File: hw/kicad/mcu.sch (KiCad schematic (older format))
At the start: 43 parts, among them P1 CONN_01X06, P2 CONN_01X03, P3 CONN_02X05, P4 CONN_01X05, SW1 PTS810, U1 STM32F446R(C-E)Tx, Y1 16 MHz

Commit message: work
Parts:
- added R43: 0R, Resistors_SMD:R_0402, symbol R
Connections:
- net +3V3: now also R43.1; no longer C9.1, U1.13 (VDDA/VREF+)
- net SWCLK: now reaches P4.2 (P2)
- net SWCLK: now also U1.49 (PA14/SYS_JTCK-SWCLK); no longer U1.46 (PA13/SYS_JTMS-SWDIO)
- net SWDIO: now reaches P4.4 (P4)
- net SWDIO: now also U1.46 (PA13/SYS_JTMS-SWDIO); no longer U1.49 (PA14/SYS_JTCK-SWCLK)
- net RST: now reaches C10.1, P4.5 (P5), U1.7 (NRST)
- new net I_SENS_V_REF: C9.1, R43.2, U1.13 (VDDA/VREF+)
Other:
- moved on the sheet: D5, D6, R12, R13, SW1
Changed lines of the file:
@@
 Text HLabel 3900 2800 0    60   Output ~ 0
 PWM_L_C
-Text HLabel 8750 4400 2    60   Output ~ 0
+Text HLabel 9300 4400 2    60   Output ~ 0
 I_SENS_V_REF
 Text HLabel 3900 4100 0    60   Input ~ 0
@@
 F 3 "" H 8550 4600 60  0000 C CNN
 	1    8550 4600
-	1    0    0    -1
-$EndComp
-$Comp
-L CONN_01X05 P4
-U 1 1 581756C8
-P 9750 1400
-F 0 "P4" H 9750 1700 50  0000 C CNN
-F 1 "CONN_01X05" V 9850 1400 50  0000 C CNN
-F 2 "Pin_Headers:Pin_Header_Straight_1x05" H 9750 1400 60  0001 C CNN
-F 3 "" H 9750 1400 60  0000 C CNN
-	1    9750 1400
-	1    0    0    -1
-$EndComp
-$Comp
-L +3.3V #PWR03
-U 1 1 58175A3D
-P 9450 950
-F 0 "#PWR03" H 9450 800 50  0001 C CNN
-F 1 "+3.3V" H 9450 1090 50  0000 C CNN
-F 2 "" H 9450 950 60  0000 C CNN
-F 3 "" H 9450 950 60  0000 C CNN
-	1    9450 950
 	1    0    0    -1
 $EndComp
@@
 	8350 4200 8200 4200
 Wire Wire Line
-	8350 3700 8350 4400
-Wire Wire Line
-	8200 3800 8350 3800
+	8200 3800 8550 3800
 Connection ~ 10000 5600
 Connection ~ 10000 6000
@@
 	8350 4900 8200 4900
 Wire Wire Line
-	8200 4400 8750 4400
-Connection ~ 8350 4200
-Wire Wire Line
-	8550 4400 8550 4450
-Connection ~ 8350 4400
+	8200 4400 9300 4400
+Wire Wire Line
+	8550 4350 8550 4450
 Connection ~ 8550 4400
 Wire Wire Line
-	8200 1300 9550 1300
-Wire Wire Line
-	9550 1200 9450 1200
-Wire Wire Line
-	9450 1200 9450 950
-Wire Wire Line
-	9550 1600 8900 1600
-Wire Wire Line
-	9450 1700 9450 1400
-Wire Wire Line
-	9450 1400 9550 1400
-Wire Wire Line
-	8900 1600 8900 1950
-Connection ~ 8900 1900
-Wire Wire Line
 	8900 2350 8900 2250
 Wire Wire Line
@@
 Wire Wire Line
 	8900 1900 8200 1900
-Wire Wire Line
-	8900 1500 9550 1500
-Wire Wire Line
-	8200 1400 8900 1400
-Wire Wire Line
-	8900 1400 8900 1500
 Wire Wire Line
 	8350 6100 8350 5950
@@
 	4700 1400 2950 1400
 Wire Wire Line
-	2950 1400 2950 2000
-Wire Wire Line
-	2950 2000 1800 2000
+	2950 2000 2950 1400
+Wire Wire Line
+	1800 2000 2950 2000
 Wire Wire Line
 	3050 2700 3050 1500
@@
 $EndComp
 $Comp
-L GND #PWR023
-U 1 1 58278102
-P 9450 1700
-F 0 "#PWR023" H 9450 1450 50  0001 C CNN
-F 1 "GND" H 9450 1550 50  0000 C CNN
-F 2 "" H 9450 1700 60  0000 C CNN
-F 3 "" H 9450 1700 60  0000 C CNN
-	1    9450 1700
-	1    0    0    -1
-$EndComp
-$Comp
 L R R1
 U 1 1 58291693
@@
 L LED D6
 U 1 1 58362F24
-P 10650 4850
-F 0 "D6" H 10650 4950 50  0000 C CNN
-F 1 "LED" H 10650 4750 50  0000 C CNN
-F 2 "LEDs:LED_0603" H 10650 4850 60  0001 C CNN
-F 3 "" H 10650 4850 60  0000 C CNN
-	1    10650 4850
+P 10550 3000
+F 0 "D6" H 10550 3100 50  0000 C CNN
+F 1 "LED" H 10550 2900 50  0000 C CNN
+F 2 "LEDs:LED_0603" H 10550 3000 60  0001 C CNN
+F 3 "" H 10550 3000 60  0000 C CNN
+	1    10550 3000
 	-1   0    0    1
 $EndComp
@@
 L LED D5
 U 1 1 583633B5
-P 10650 4550
-F 0 "D5" H 10650 4650 50  0000 C CNN
-F 1 "LED" H 10650 4450 50  0000 C CNN
-F 2 "LEDs:LED_0603" H 10650 4550 60  0001 C CNN
-F 3 "" H 10650 4550 60  0000 C CNN
-	1    10650 4550
+P 10550 2700
+F 0 "D5" H 10550 2800 50  0000 C CNN
+F 1 "LED" H 10550 2600 50  0000 C CNN
+F 2 "LEDs:LED_0603" H 10550 2700 60  0001 C CNN
+F 3 "" H 10550 2700 60  0000 C CNN
+	1    10550 2700
 	-1   0    0    1
 $EndComp
 Wire Wire Line
-	10850 4550 11000 4550
-Wire Wire Line
-	11000 4550 11000 4950
-Wire Wire Line
-	10850 4850 11000 4850
-Connection ~ 11000 4850
+	10750 2700 10900 2700
+Wire Wire Line
+	10900 2700 10900 3100
+Wire Wire Line
+	10750 3000 10900 3000
+Connection ~ 10900 3000
 $Comp
 L GND #PWR028
 U 1 1 58363604
-P 11000 4950
-F 0 "#PWR028" H 11000 4700 50  0001 C CNN
-F 1 "GND" H 11000 4800 50  0000 C CNN
-F 2 "" H 11000 4950 60  0000 C CNN
-F 3 "" H 11000 4950 60  0000 C CNN
-	1    11000 4950
+P 10900 3100
+F 0 "#PWR028" H 10900 2850 50  0001 C CNN
+F 1 "GND" H 10900 2950 50  0000 C CNN
+F 2 "" H 10900 3100 60  0000 C CNN
+F 3 "" H 10900 3100 60  0000 C CNN
+	1    10900 3100
 	1    0    0    -1
 $EndComp
@@
 L R R12
 U 1 1 58363C15
-P 10250 4550
-F 0 "R12" V 10330 4550 50  0000 C CNN
-F 1 "100R" V 10250 4550 50  0000 C CNN
-F 2 "Resistors_SMD:R_0402" V 10180 4550 30  0001 C CNN
-F 3 "" H 10250 4550 30  0000 C CNN
-	1    10250 4550
+P 10150 2700
+F 0 "R12" V 10230 2700 50  0000 C CNN
+F 1 "100R" V 10150 2700 50  0000 C CNN
+F 2 "Resistors_SMD:R_0402" V 10080 2700 30  0001 C CNN
+F 3 "" H 10150 2700 30  0000 C CNN
+	1    10150 2700
 	0    1    1    0
 $EndComp
@@
 L R R13
 U 1 1 58363D14
-P 10250 4850
-F 0 "R13" V 10330 4850 50  0000 C CNN
-F 1 "100R" V 10250 4850 50  0000 C CNN
-F 2 "Resistors_SMD:R_0402" V 10180 4850 30  0001 C CNN
-F 3 "" H 10250 4850 30  0000 C CNN
-	1    10250 4850
+P 10150 3000
+F 0 "R13" V 10230 3000 50  0000 C CNN
+F 1 "100R" V 10150 3000 50  0000 C CNN
+F 2 "Resistors_SMD:R_0402" V 10080 3000 30  0001 C CNN
+F 3 "" H 10150 3000 30  0000 C CNN
+	1    10150 3000
 	0    1    1    0
 $EndComp
 Wire Wire Line
-	10400 4850 10450 4850
-Wire Wire Line
-	10400 4550 10450 4550
-Text Label 9800 4550 0    60   ~ 0
+	10300 3000 10350 3000
+Wire Wire Line
+	10300 2700 10350 2700
+Text Label 9700 2700 0    60   ~ 0
 LED_R
 Wire Wire Line
-	9800 4550 10100 4550
-Wire Wire Line
-	10100 4850 9800 4850
-Text Label 9800 4850 0    60   ~ 0
+	9700 2700 10000 2700
+Wire Wire Line
+	10000 3000 9700 3000
+Text Label 9700 3000 0    60   ~ 0
 LED_G
 Wire Wire Line
@@
 L PTS810 SW1
 U 1 1 583BCE20
-P 10650 4100
-F 0 "SW1" H 10650 4200 40  0000 C CNN
-F 1 "PTS810" H 10650 4050 40  0000 C CNN
-F 2 "electromechanical:PTS810" H 10650 4100 60  0001 C CNN
-F 3 "" H 10650 4100 60  0000 C CNN
-	1    10650 4100
+P 10550 2250
+F 0 "SW1" H 10550 2350 40  0000 C CNN
+F 1 "PTS810" H 10550 2200 40  0000 C CNN
+F 2 "electromechanical:PTS810" H 10550 2250 60  0001 C CNN
+F 3 "" H 10550 2250 60  0000 C CNN
+	1    10550 2250
 	1    0    0    -1
 $EndComp
@@
 L GND #PWR034
 U 1 1 583BE21E
-P 11000 4200
-F 0 "#PWR034" H 11000 3950 50  0001 C CNN
-F 1 "GND" H 11000 4050 50  0000 C CNN
-F 2 "" H 11000 4200 60  0000 C CNN
-F 3 "" H 11000 4200 60  0000 C CNN
-	1    11000 4200
-	1    0    0    -1
-$EndComp
-Wire Wire Line
-	10750 4100 11000 4100
-Wire Wire Line
-	11000 4100 11000 4200
-Wire Wire Line
-	10550 4100 9800 4100
-Text Label 9800 4100 0    60   ~ 0
+P 10900 2350
+F 0 "#PWR034" H 10900 2100 50  0001 C CNN
+F 1 "GND" H 10900 2200 50  0000 C CNN
+F 2 "" H 10900 2350 60  0000 C CNN
+F 3 "" H 10900 2350 60  0000 C CNN
+	1    10900 2350
+	1    0    0    -1
+$EndComp
+Wire Wire Line
+	10650 2250 10900 2250
+Wire Wire Line
+	10900 2250 10900 2350
+Wire Wire Line
+	10450 2250 9700 2250
+Text Label 9700 2250 0    60   ~ 0
 BTN
+$Comp
+L GND #PWR?
+U 1 1 5842C05B
+P 10450 1400
+F 0 "#PWR?" H 10450 1150 50  0001 C CNN
+F 1 "GND" H 10450 1250 50  0000 C CNN
+F 2 "" H 10450 1400 60  0000 C CNN
+F 3 "" H 10450 1400 60  0000 C CNN
+	1    10450 1400
+	0    1    1    0
+$EndComp
+$Comp
+L +3.3V #PWR?
+U 1 1 5842C60A
+P 10400 1150
+F 0 "#PWR?" H 10400 1000 50  0001 C CNN
+F 1 "+3.3V" H 10400 1290 50  0000 C CNN
+F 2 "" H 10400 1150 60  0000 C CNN
+F 3 "" H 10400 1150 60  0000 C CNN
+	1    10400 1150
+	1    0    0    -1
+$EndComp
+Text Label 9950 1500 0    60   ~ 0
+SWDIO
+Text Label 9950 1300 0    60   ~ 0
+SWCLK
+Text Label 9950 1600 0    60   ~ 0
+RST
+Wire Wire Line
+	8900 1900 8900 1950
+Text Label 8800 1300 2    60   ~ 0
+SWDIO
+Text Label 8800 1400 2    60   ~ 0
+SWCLK
+Text Label 8800 1900 2    60   ~ 0
+RST
+Wire Wire Line
+	8200 1300 8800 1300
+Wire Wire Line
+	8200 1400 8800 1400
+$Comp
+L R R43
+U 1 1 58432E11
+P 8550 4200
+F 0 "R43" H 8700 4200 50  0000 C CNN
+F 1 "0R" V 8550 4200 50  0000 C CNN
+F 2 "Resistors_SMD:R_0402" V 8480 4200 30  0001 C CNN
+F 3 "" H 8550 4200 30  0000 C CNN
+	1    8550 4200
+	1    0    0    -1
+$EndComp
+Wire Wire Line
+	8350 3700 8350 4200
+Wire Wire Line
+	8550 3800 8550 4050
+Text Label 8650 4400 0    60   ~ 0
+I_SENS_V_REF
+$Comp
+L CONN_01X05 P4
+U 1 1 584386F1
+P 10650 1400
+F 0 "P4" H 10650 1700 50  0000 C CNN
+F 1 "CONN_01X05" V 10750 1400 50  0000 C CNN
+F 2 "Pin_Headers:Pin_Header_Straight_1x05" H 10650 1400 60  0001 C CNN
+F 3 "" H 10650 1400 60  0000 C CNN
+	1    10650 1400
+	1    0    0    -1
+$EndComp
+Wire Wire Line
+	9950 1300 10450 1300
+Wire Wire Line
+	9950 1500 10450 1500
+Wire Wire Line
+	9950 1600 10450 1600
+Wire Wire Line
+	10400 1150 10400 1200
+Wire Wire Line
+	10400 1200 10450 1200
 $EndSCHEMATC

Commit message: Aligned, started rework current shunt layout and copper pour
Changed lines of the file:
@@
 $EndComp
 $Comp
-L +3.3V #PWR04
+L +3.3V #PWR03
 U 1 1 5821B0F1
 P 1600 3450
-F 0 "#PWR04" H 1600 3300 50  0001 C CNN
+F 0 "#PWR03" H 1600 3300 50  0001 C CNN
 F 1 "+3.3V" H 1600 3590 50  0000 C CNN
 F 2 "" H 1600 3450 60  0000 C CNN
@@
 $EndComp
 $Comp
-L +3.3V #PWR05
+L +3.3V #PWR04
 U 1 1 5821BAD6
 P 2050 2350
-F 0 "#PWR05" H 2050 2200 50  0001 C CNN
+F 0 "#PWR04" H 2050 2200 50  0001 C CNN
 F 1 "+3.3V" H 2050 2490 50  0000 C CNN
 F 2 "" H 2050 2350 60  0000 C CNN
@@
 $EndComp
 $Comp
-L +3.3V #PWR06
+L +3.3V #PWR05
 U 1 1 5821C068
 P 2450 1650
-F 0 "#PWR06" H 2450 1500 50  0001 C CNN
+F 0 "#PWR05" H 2450 1500 50  0001 C CNN
 F 1 "+3.3V" H 2450 1790 50  0000 C CNN
 F 2 "" H 2450 1650 60  0000 C CNN
@@
 $EndComp
 $Comp
-L +3.3V #PWR07
+L +3.3V #PWR06
 U 1 1 5821C7C9
 P 2050 950
-F 0 "#PWR07" H 2050 800 50  0001 C CNN
+F 0 "#PWR06" H 2050 800 50  0001 C CNN
 F 1 "+3.3V" H 2050 1090 50  0000 C CNN
 F 2 "" H 2050 950 60  0000 C CNN
@@
 $EndComp
 $Comp
-L +5V #PWR08
+L +5V #PWR07
 U 1 1 5823D67C
 P 1650 6750
-F 0 "#PWR08" H 1650 6600 50  0001 C CNN
+F 0 "#PWR07" H 1650 6600 50  0001 C CNN
 F 1 "+5V" H 1650 6890 50  0000 C CNN
 F 2 "" H 1650 6750 60  0000 C CNN
@@
 	4700 1400 2950 1400
 Wire Wire Line
-	2950 2000 2950 1400
-Wire Wire Line
-	1800 2000 2950 2000
+	2950 1400 2950 2000
+Wire Wire Line
+	2950 2000 1800 2000
 Wire Wire Line
 	3050 2700 3050 1500
@@
 Connection ~ 2950 7100
 $Comp
-L +3.3V #PWR09
+L +3.3V #PWR08
 U 1 1 5823F97D
 P 1950 5650
-F 0 "#PWR09" H 1950 5500 50  0001 C CNN
+F 0 "#PWR08" H 1950 5500 50  0001 C CNN
 F 1 "+3.3V" H 1950 5790 50  0000 C CNN
 F 2 "" H 1950 5650 60  0000 C CNN
@@
 HALL_3
 $Comp
-L GND #PWR010
+L GND #PWR09
 U 1 1 5827704E
 P 2050 1650
-F 0 "#PWR010" H 2050 1400 50  0001 C CNN
+F 0 "#PWR09" H 2050 1400 50  0001 C CNN
 F 1 "GND" H 2050 1500 50  0000 C CNN
 F 2 "" H 2050 1650 60  0000 C CNN
@@
 $EndComp
 $Comp
-L GND #PWR011
+L GND #PWR010
 U 1 1 58277258
 P 2450 2350
-F 0 "#PWR011" H 2450 2100 50  0001 C CNN
+F 0 "#PWR010" H 2450 2100 50  0001 C CNN
 F 1 "GND" H 2450 2200 50  0000 C CNN
 F 2 "" H 2450 2350 60  0000 C CNN
@@
 $EndComp
 $Comp
-L GND #PWR012
+L GND #PWR011
 U 1 1 582772CC
 P 2050 3050
-F 0 "#PWR012" H 2050 2800 50  0001 C CNN
+F 0 "#PWR011" H 2050 2800 50  0001 C CNN
 F 1 "GND" H 2050 2900 50  0000 C CNN
 F 2 "" H 2050 3050 60  0000 C CNN
@@
 $EndComp
 $Comp
-L GND #PWR013
+L GND #PWR012
 U 1 1 58277340
 P 1600 4150
-F 0 "#PWR013" H 1600 3900 50  0001 C CNN
+F 0 "#PWR012" H 1600 3900 50  0001 C CNN
 F 1 "GND" H 1600 4000 50  0000 C CNN
 F 2 "" H 1600 4150 60  0000 C CNN
@@
 $EndComp
 $Comp
-L GND #PWR014
+L GND #PWR013
 U 1 1 582774EF
 P 2950 7150
-F 0 "#PWR014" H 2950 6900 50  0001 C CNN
+F 0 "#PWR013" H 2950 6900 50  0001 C CNN
 F 1 "GND" H 2950 7000 50  0000 C CNN
 F 2 "" H 2950 7150 60  0000 C CNN
@@
 $EndComp
 $Comp
-L GND #PWR015
+L GND #PWR014
 U 1 1 58277759
 P 1650 6250
-F 0 "#PWR015" H 1650 6000 50  0001 C CNN
+F 0 "#PWR014" H 1650 6000 50  0001 C CNN
 F 1 "GND" H 1650 6100 50  0000 C CNN
 F 2 "" H 1650 6250 60  0000 C CNN
@@
 $EndComp
 $Comp
-L GND #PWR016
+L GND #PWR015
 U 1 1 582779AA
 P 10000 6100
-F 0 "#PWR016" H 10000 5850 50  0001 C CNN
+F 0 "#PWR015" H 10000 5850 50  0001 C CNN
 F 1 "GND" H 10000 5950 50  0000 C CNN
 F 2 "" H 10000 6100 60  0000 C CNN
@@
 $EndComp
 $Comp
-L GND #PWR017
+L GND #PWR016
 U 1 1 58277BF1
 P 8350 6100
-F 0 "#PWR017" H 8350 5850 50  0001 C CNN
+F 0 "#PWR016" H 8350 5850 50  0001 C CNN
 F 1 "GND" H 8350 5950 50  0000 C CNN
 F 2 "" H 8350 6100 60  0000 C CNN
@@
 $EndComp
 $Comp
-L GND #PWR018
+L GND #PWR017
 U 1 1 58277C89
 P 8350 5150
-F 0 "#PWR018" H 8350 4900 50  0001 C CNN
+F 0 "#PWR017" H 8350 4900 50  0001 C CNN
 F 1 "GND" H 8350 5000 50  0000 C CNN
 F 2 "" H 8350 5150 60  0000 C CNN
@@
 $EndComp
 $Comp
-L GND #PWR019
+L GND #PWR018
 U 1 1 58277D21
 P 8550 4750
-F 0 "#PWR019" H 8550 4500 50  0001 C CNN
+F 0 "#PWR018" H 8550 4500 50  0001 C CNN
 F 1 "GND" H 8550 4600 50  0000 C CNN
 F 2 "" H 8550 4750 60  0000 C CNN
@@
 $EndComp
 $Comp
-L GND #PWR020
+L GND #PWR019
 U 1 1 58277E8B
 P 9650 3400
-F 0 "#PWR020" H 9650 3150 50  0001 C CNN
+F 0 "#PWR019" H 9650 3150 50  0001 C CNN
 F 1 "GND" H 9650 3250 50  0000 C CNN
 F 2 "" H 9650 3400 60  0000 C CNN
@@
 $EndComp
 $Comp
-L GND #PWR021
+L GND #PWR020
 U 1 1 58277FF6
 P 8350 2350
-F 0 "#PWR021" H 8350 2100 50  0001 C CNN
+F 0 "#PWR020" H 8350 2100 50  0001 C CNN
 F 1 "GND" H 8350 2200 50  0000 C CNN
 F 2 "" H 8350 2350 60  0000 C CNN
@@
 $EndComp
 $Comp
-L GND #PWR022
+L GND #PWR021
 U 1 1 5827806A
 P 8900 2350
-F 0 "#PWR022" H 8900 2100 50  0001 C CNN
+F 0 "#PWR021" H 8900 2100 50  0001 C CNN
 F 1 "GND" H 8900 2200 50  0000 C CNN
 F 2 "" H 8900 2350 60  0000 C CNN
@@
 $EndComp
 $Comp
-L VPP #PWR024
+L VPP #PWR022
 U 1 1 582916A9
 P 900 3250
-F 0 "#PWR024" H 900 3100 50  0001 C CNN
+F 0 "#PWR022" H 900 3100 50  0001 C CNN
 F 1 "VPP" H 900 3400 50  0000 C CNN
 F 2 "" H 900 3250 60  0000 C CNN
@@
 	900  4250 900  4350
 $Comp
-L GND #PWR025
+L GND #PWR023
 U 1 1 582916B5
 P 1050 4450
-F 0 "#PWR025" H 1050 4200 50  0001 C CNN
+F 0 "#PWR023" H 1050 4200 50  0001 C CNN
 F 1 "GND" H 1050 4300 50  0000 C CNN
 F 2 "" H 1050 4450 60  0000 C CNN
@@
 $EndComp
 $Comp
-L +3.3V #PWR026
+L +3.3V #PWR024
 U 1 1 5833D72B
 P 900 4950
-F 0 "#PWR026" H 900 4800 50  0001 C CNN
+F 0 "#PWR024" H 900 4800 50  0001 C CNN
 F 1 "+3.3V" H 900 5090 50  0000 C CNN
 F 2 "" H 900 4950 60  0000 C CNN
@@
 	900  5050 900  4950
 $Comp
-L GND #PWR027
+L GND #PWR025
 U 1 1 5833D8AB
 P 900 5850
-F 0 "#PWR027" H 900 5600 50  0001 C CNN
+F 0 "#PWR025" H 900 5600 50  0001 C CNN
 F 1 "GND" H 900 5700 50  0000 C CNN
 F 2 "" H 900 5850 60  0000 C CNN
@@
 Connection ~ 10900 3000
 $Comp
-L GND #PWR028
+L GND #PWR026
 U 1 1 58363604
 P 10900 3100
-F 0 "#PWR028" H 10900 2850 50  0001 C CNN
+F 0 "#PWR026" H 10900 2850 50  0001 C CNN
 F 1 "GND" H 10900 2950 50  0000 C CNN
 F 2 "" H 10900 3100 60  0000 C CNN
@@
 $EndComp
 $Comp
-L +5V #PWR029
+L +5V #PWR027
 U 1 1 58398559
 P 1650 7150
-F 0 "#PWR029" H 1650 7000 50  0001 C CNN
+F 0 "#PWR027" H 1650 7000 50  0001 C CNN
 F 1 "+5V" H 1650 7290 50  0000 C CNN
 F 2 "" H 1650 7150 60  0000 C CNN
@@
 	2250 7050 2250 7150
 $Comp
-L GND #PWR030
+L GND #PWR028
 U 1 1 58399288
 P 2250 7550
-F 0 "#PWR030" H 2250 7300 50  0001 C CNN
+F 0 "#PWR028" H 2250 7300 50  0001 C CNN
 F 1 "GND" H 2250 7400 50  0000 C CNN
 F 2 "" H 2250 7550 60  0000 C CNN
@@
 $EndComp
 $Comp
-L +3.3V #PWR031
+L +3.3V #PWR029
 U 1 1 5839AEF9
 P 6150 6700
-F 0 "#PWR031" H 6150 6550 50  0001 C CNN
+F 0 "#PWR029" H 6150 6550 50  0001 C CNN
 F 1 "+3.3V" H 6150 6840 50  0000 C CNN
 F 2 "" H 6150 6700 60  0000 C CNN
@@
 $EndComp
 $Comp
-L GND #PWR032
+L GND #PWR030
 U 1 1 5839AF82
 P 6150 7400
-F 0 "#PWR032" H 6150 7150 50  0001 C CNN
+F 0 "#PWR030" H 6150 7150 50  0001 C CNN
 F 1 "GND" H 6150 7250 50  0000 C CNN
 F 2 "" H 6150 7400 60  0000 C CNN
@@
 $EndComp
 $Comp
-L +5V #PWR033
+L +5V #PWR031
 U 1 1 5839B00B
 P 6250 6800
-F 0 "#PWR033" H 6250 6650 50  0001 C CNN
+F 0 "#PWR031" H 6250 6650 50  0001 C CNN
 F 1 "+5V" H 6250 6940 50  0000 C CNN
 F 2 "" H 6250 6800 60  0000 C CNN
@@
 $EndComp
 $Comp
-L GND #PWR034
+L GND #PWR032
 U 1 1 583BE21E
 P 10900 2350
-F 0 "#PWR034" H 10900 2100 50  0001 C CNN
+F 0 "#PWR032" H 10900 2100 50  0001 C CNN
 F 1 "GND" H 10900 2200 50  0000 C CNN
 F 2 "" H 10900 2350 60  0000 C CNN
@@
 BTN
 $Comp
-L GND #PWR?
+L GND #PWR033
 U 1 1 5842C05B
 P 10450 1400
-F 0 "#PWR?" H 10450 1150 50  0001 C CNN
+F 0 "#PWR033" H 10450 1150 50  0001 C CNN
 F 1 "GND" H 10450 1250 50  0000 C CNN
 F 2 "" H 10450 1400 60  0000 C CNN
@@
 $EndComp
 $Comp
-L +3.3V #PWR?
+L +3.3V #PWR034
 U 1 1 5842C60A
 P 10400 1150
-F 0 "#PWR?" H 10400 1000 50  0001 C CNN
+F 0 "#PWR034" H 10400 1000 50  0001 C CNN
 F 1 "+3.3V" H 10400 1290 50  0000 C CNN
 F 2 "" H 10400 1150 60  0000 C CNN

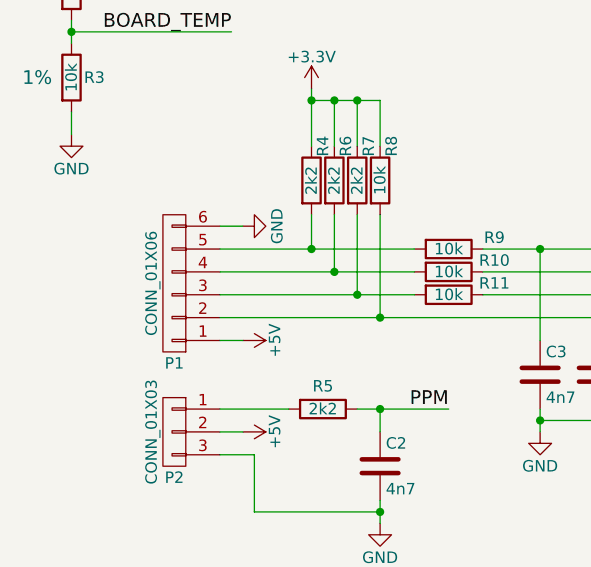
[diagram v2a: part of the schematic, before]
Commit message: Changed footprint of hall sensor contact and placed more components
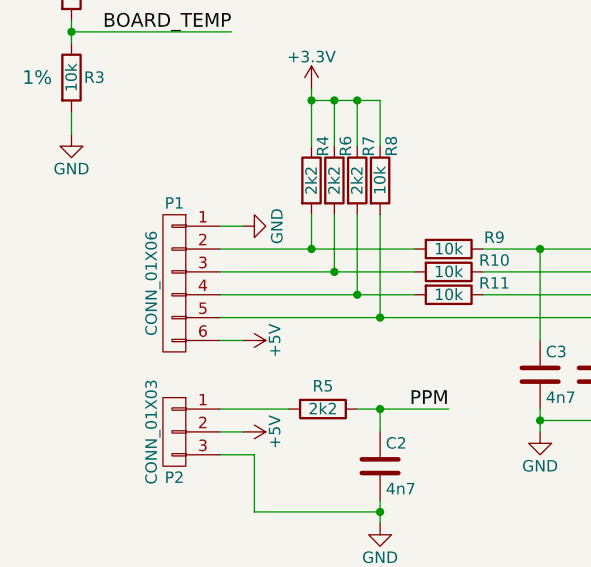
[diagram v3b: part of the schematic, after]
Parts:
- P1: footprint Pin_Headers:Pin_Header_Straight_1x06 -> Micro_JST:Micro_JST_p2.0_6
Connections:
- net +5V: now also P1.6 (P6); no longer P1.1 (P1)
- net GND: now also P1.1 (P1); no longer P1.6 (P6)
- net MOT_TEMP: now also P1.5 (P5); no longer P1.2 (P2)
- net at R11.2, R7.2: now also P1.4 (P4); no longer P1.3 (P3)
- net at R10.2, R6.2: now also P1.3 (P3); no longer P1.4 (P4)
- net at R4.2, R9.2: now also P1.2 (P2); no longer P1.5 (P5)
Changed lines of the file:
@@
 F 0 "P1" H 1350 6850 50  0000 C CNN
 F 1 "CONN_01X06" V 1450 6500 50  0000 C CNN
-F 2 "Pin_Headers:Pin_Header_Straight_1x06" H 1350 6500 60  0001 C CNN
+F 2 "Micro_JST:Micro_JST_p2.0_6" H 1350 6500 60  0001 C CNN
 F 3 "" H 1350 6500 60  0000 C CNN
 	1    1350 6500
-	-1   0    0    1
+	-1   0    0    -1
 $EndComp
 $Comp

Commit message: Routed power supply
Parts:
- P1: footprint Micro_JST:Micro_JST_p2.0_6 -> JST_ZH:JST_ZH_B6B-ZR
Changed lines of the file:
@@
 F 0 "P1" H 1350 6850 50  0000 C CNN
 F 1 "CONN_01X06" V 1450 6500 50  0000 C CNN
-F 2 "Micro_JST:Micro_JST_p2.0_6" H 1350 6500 60  0001 C CNN
+F 2 "JST_ZH:JST_ZH_B6B-ZR" H 1350 6500 60  0001 C CNN
 F 3 "" H 1350 6500 60  0000 C CNN
 	1    1350 6500

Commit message: Routed EMF and I sense to mcu
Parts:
- removed R43: 0R, Resistors_SMD:R_0402, symbol R
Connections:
- net I_SENS_V_REF is gone; now on net +3V3: C9.1, U1.13 (VDDA/VREF+)
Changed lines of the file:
@@
 	8200 4400 9300 4400
 Wire Wire Line
-	8550 4350 8550 4450
+	8550 3800 8550 4450
 Connection ~ 8550 4400
 Wire Wire Line
@@
 Wire Wire Line
 	8200 1400 8800 1400
-$Comp
-L R R43
-U 1 1 58432E11
-P 8550 4200
-F 0 "R43" H 8700 4200 50  0000 C CNN
-F 1 "0R" V 8550 4200 50  0000 C CNN
-F 2 "Resistors_SMD:R_0402" V 8480 4200 30  0001 C CNN
-F 3 "" H 8550 4200 30  0000 C CNN
-	1    8550 4200
-	1    0    0    -1
-$EndComp
 Wire Wire Line
 	8350 3700 8350 4200
-Wire Wire Line
-	8550 3800 8550 4050
-Text Label 8650 4400 0    60   ~ 0
-I_SENS_V_REF
 $Comp
 L CONN_01X05 P4

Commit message: First draft of completely routed board
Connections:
- net +3V3: now also P3.4 (P4); no longer P3.2 (P2)
- net +5V: now also P3.2 (P2); no longer P3.4 (P4)
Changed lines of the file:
@@
 L +3.3V #PWR029
 U 1 1 5839AEF9
-P 6150 6700
-F 0 "#PWR029" H 6150 6550 50  0001 C CNN
-F 1 "+3.3V" H 6150 6840 50  0000 C CNN
-F 2 "" H 6150 6700 60  0000 C CNN
-F 3 "" H 6150 6700 60  0000 C CNN
-	1    6150 6700
+P 6250 6800
+F 0 "#PWR029" H 6250 6650 50  0001 C CNN
+F 1 "+3.3V" H 6250 6940 50  0000 C CNN
+F 2 "" H 6250 6800 60  0000 C CNN
+F 3 "" H 6250 6800 60  0000 C CNN
+	1    6250 6800
 	1    0    0    -1
 $EndComp
@@
 L +5V #PWR031
 U 1 1 5839B00B
-P 6250 6800
-F 0 "#PWR031" H 6250 6650 50  0001 C CNN
-F 1 "+5V" H 6250 6940 50  0000 C CNN
-F 2 "" H 6250 6800 60  0000 C CNN
-F 3 "" H 6250 6800 60  0000 C CNN
-	1    6250 6800
+P 6150 6700
+F 0 "#PWR031" H 6150 6550 50  0001 C CNN
+F 1 "+5V" H 6150 6840 50  0000 C CNN
+F 2 "" H 6150 6700 60  0000 C CNN
+F 3 "" H 6150 6700 60  0000 C CNN
+	1    6150 6700
 	1    0    0    -1
 $EndComp

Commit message: Forgot some traces...
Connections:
- net BTN: now also U1.28 (PB2/BOOT1)
- net GATE_PWR_EN: now also U1.17 (PA3/ADC123_IN3)
- net LED_G: now also U1.29 (PB10)
- net LED_R: now also U1.51 (PC10)
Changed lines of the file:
@@
 $EndComp
 Wire Wire Line
-	8350 2300 8200 2300
+	8650 2300 8200 2300
 Wire Wire Line
 	9000 6000 9000 5950
@@
 	8900 2350 8900 2250
 Wire Wire Line
-	8350 2350 8350 2300
+	8650 2350 8650 2300
 Wire Wire Line
 	8900 1900 8200 1900
@@
 	4700 1400 2950 1400
 Wire Wire Line
-	2950 1400 2950 2000
-Wire Wire Line
-	2950 2000 1800 2000
+	2950 2000 2950 1400
+Wire Wire Line
+	1800 2000 2950 2000
 Wire Wire Line
 	3050 2700 3050 1500
@@
 L GND #PWR020
 U 1 1 58277FF6
-P 8350 2350
-F 0 "#PWR020" H 8350 2100 50  0001 C CNN
-F 1 "GND" H 8350 2200 50  0000 C CNN
-F 2 "" H 8350 2350 60  0000 C CNN
-F 3 "" H 8350 2350 60  0000 C CNN
-	1    8350 2350
+P 8650 2350
+F 0 "#PWR020" H 8650 2100 50  0001 C CNN
+F 1 "GND" H 8650 2200 50  0000 C CNN
+F 2 "" H 8650 2350 60  0000 C CNN
+F 3 "" H 8650 2350 60  0000 C CNN
+	1    8650 2350
 	1    0    0    -1
 $EndComp
@@
 Text Notes 950  3800 0    39   ~ 0
 G ≈ 3.3/40 V/V
-Text HLabel 3300 3350 0    60   Output ~ 0
+Text HLabel 3900 1600 0    60   Output ~ 0
 GATE_PWR_EN
 Wire Wire Line
@@
 Wire Wire Line
 	10400 1200 10450 1200
+Wire Wire Line
+	3900 1600 4700 1600
+Text Label 3900 5000 0    60   ~ 0
+LED_R
+Wire Wire Line
+	3900 3400 4700 3400
+Wire Wire Line
+	3900 5000 4700 5000
+Text Label 3900 3400 0    60   ~ 0
+LED_G
+Text Label 8500 2400 2    60   ~ 0
+BTN
+Wire Wire Line
+	8500 2400 8200 2400
 $EndSCHEMATC
